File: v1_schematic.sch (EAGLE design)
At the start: 114 parts, among them IC1 PCA82C250, IC2 FT232RL, IC3 SP3223EBP, IC4 MAX481CPA, IC5 LM2576T, Q1 25MHz, Q2 32.768kHz, Q3 2N2222A, T1 ST02-3.5MM, T3 2N2222, T4 2N2222, T5 2N2222, T6 2N2222, T7 2N2222, U1 ON_SEMICONDUCTOR_NCP1117ST33T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, U2 ON_SEMICONDUCTOR_NCP1117ST50T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, X1 MINI-USB-32005-201

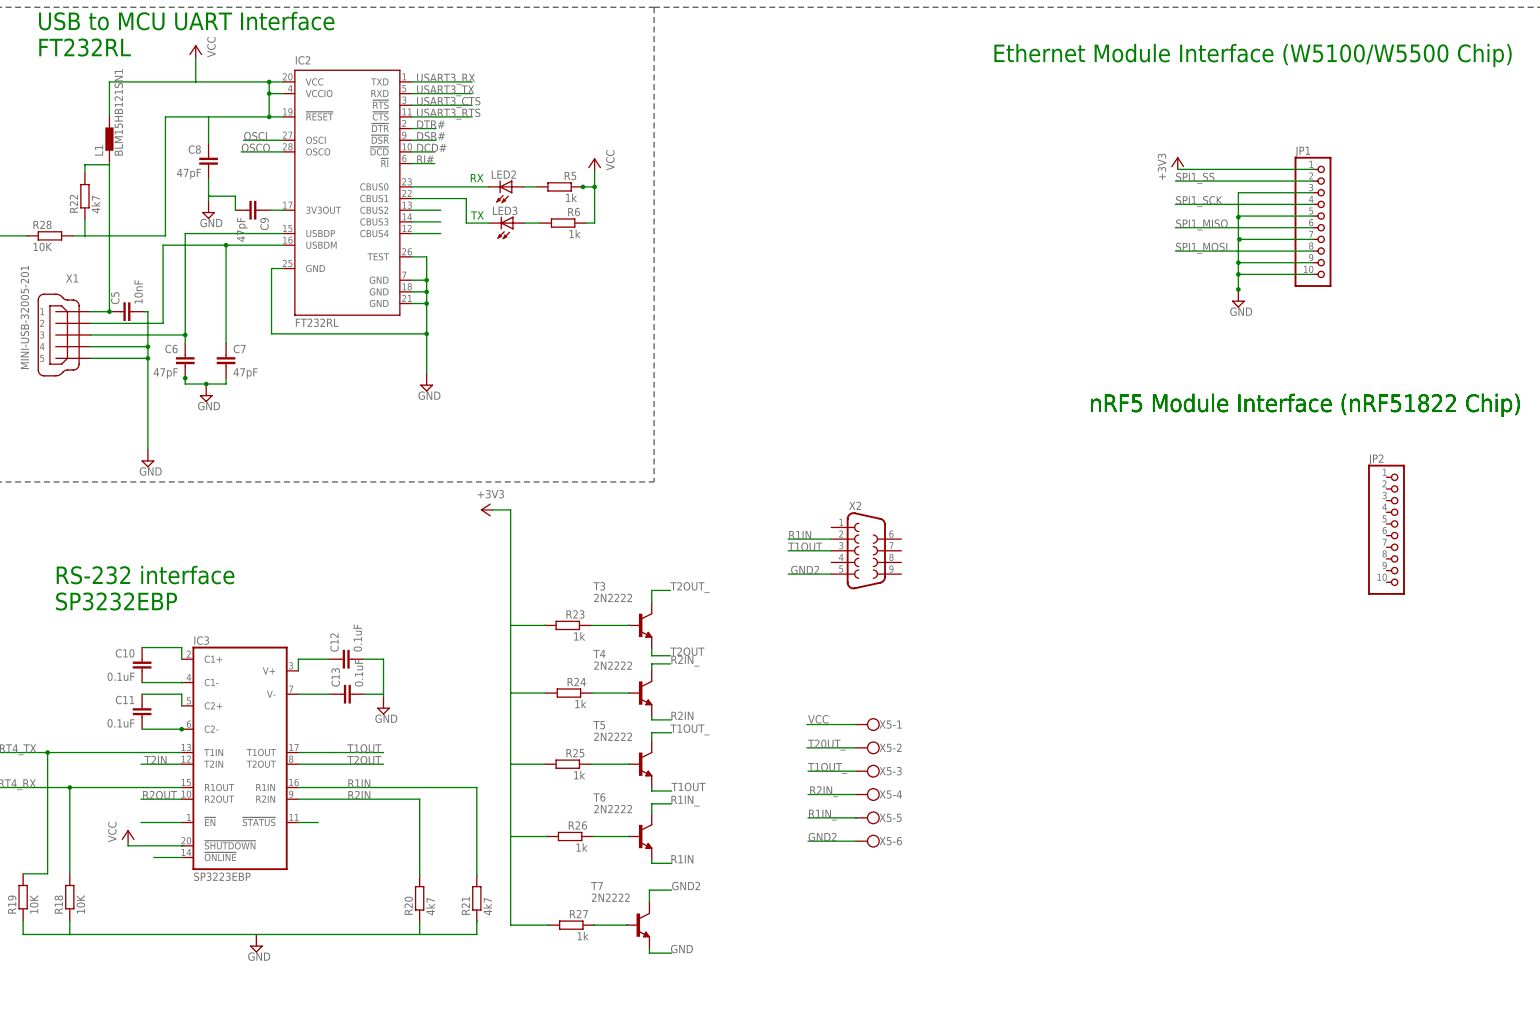
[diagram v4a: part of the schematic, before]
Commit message: SD Card Interface
- Added SD card interface based on
SD MEMORY CARD PUSH-PUSH WITH CONNECTOR TYPE B
Package Type: SDBMF-009XXBXX2
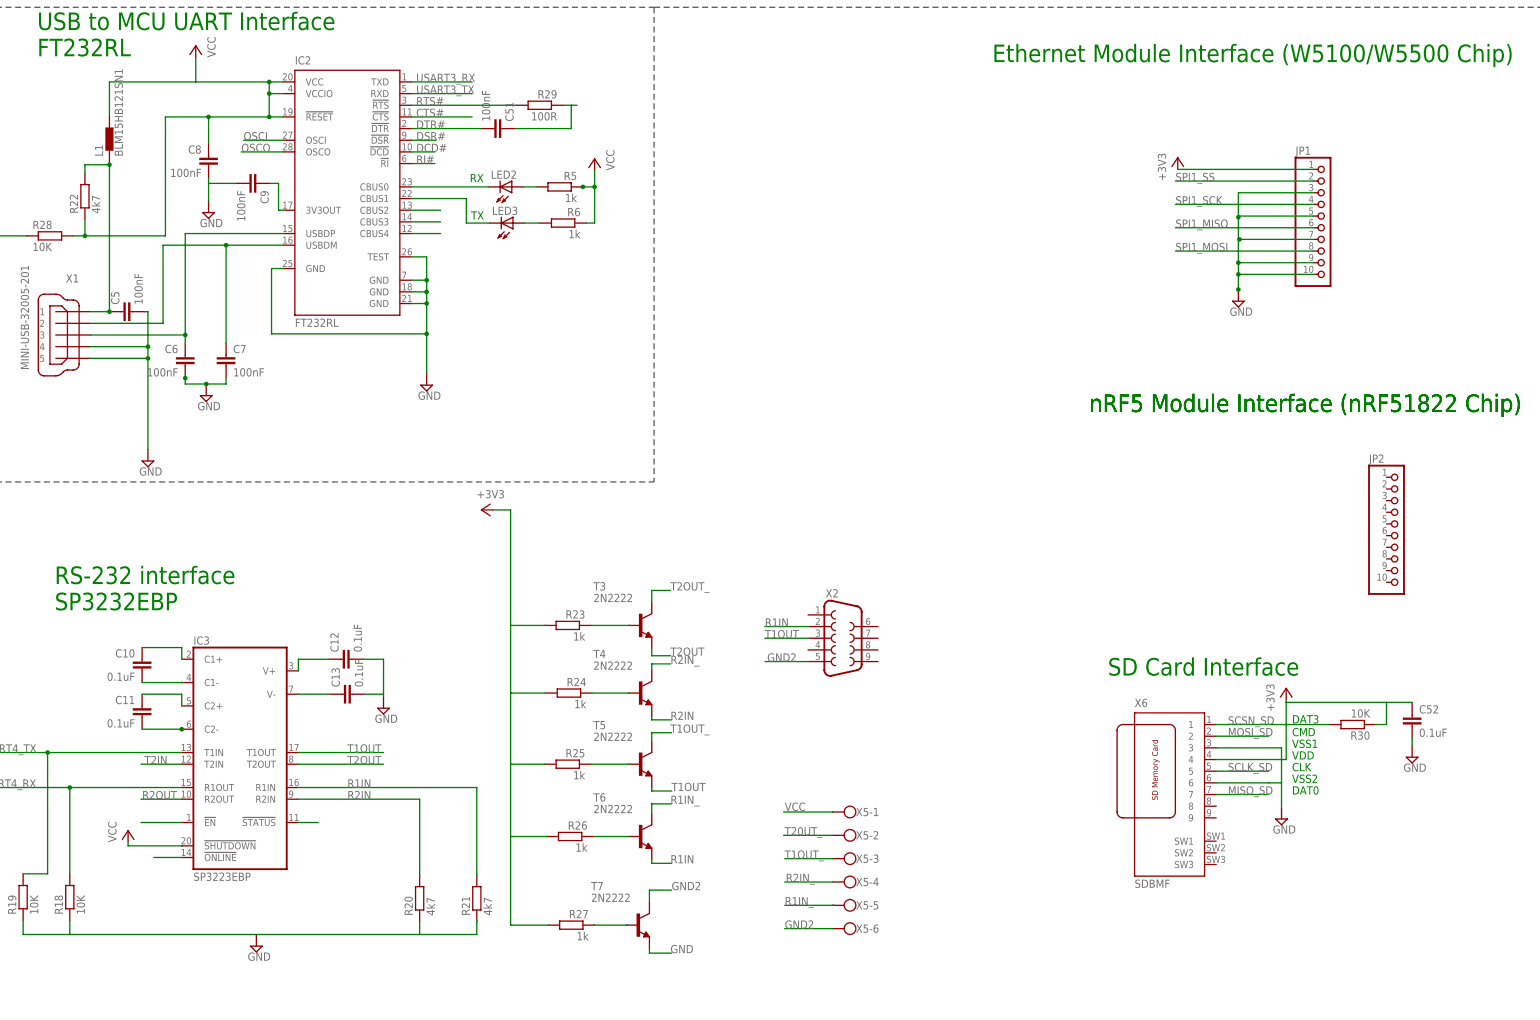
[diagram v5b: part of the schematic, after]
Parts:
- added C51: 100nF, resistor:C-EUC0805
- added C52: 0.1uF, resistor:C-EUC0805
- added R29: 100R, resistor:R-EU_R0805
- added R30: 10K, rcl:R-EU_R0805
- added X6: SDBMF, farnell:SDBMF
- C5: value 10nF -> 100nF
- C6, C7, C8, C9: value 47pF -> 100nF
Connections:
- new net CTS#: IC2.!CTS
- new net MISO_SD: X6.7
- new net MOSI_SD: X6.2
- new net RTS#: IC2.!RTS, R29.2
- new net SCLK_SD: X6.5
- new net SCSN_SD: R30.2, X6.1
- net +3V3: now also C52.1, R30.1, X6.4
- net DTR#: now also C51.2
- net GND: now also C52.2, X6.3, X6.6
- net N$31: now also C51.1, R29.1; no longer R22.1, R28.2
- net N$9: now also IC2.3V3OUT
- net USART3_CTS: no longer IC2.!RTS
- net USART3_RTS: no longer IC2.!CTS
- net VCC: now also R22.1, R28.2
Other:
- note added: "CLK"
- note added: "CMD"
- note added: "DAT0"
- note added: "DAT3"
- note added: "SD Card Interface"
- note added: "VDD"
- note added: "VSS1"
- note added: "VSS2"
- moved on the sheet: C9, X2, X5-1, X5-2, X5-3, X5-4, X5-5, X5-6

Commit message: Corrections
- Adjusted FT2323 interface to USART1 and completed Interface connections
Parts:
- removed JP1, JP2: (no value), pinhead:PINHD-1X10
- added X7, X8: 5566-8, con-molex:5566-8
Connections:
- removed net N$1: U$1.NRST
- removed net N$31: C51.1, R29.1
- removed net SPI1_MISO: JP1.6, U$1.PA6
- removed net SPI1_MOSI: JP1.8, U$1.PA7
- removed net SPI1_SCK: JP1.4, U$1.PA5
- removed net SPI1_SS: JP1.2, U$1.PA4
- new net ETH_MISO: U$1.PA6, X8-7.S
- new net ETH_MOSI: U$1.PA7, X8-6.S
- new net ETH_SCK: U$1.PA5, X8-4.S
- new net ETH_SS: U$1.PA4, X8-3.S
- new net NRF_CE: X7-3.S
- new net NRF_CS: X7-4.S
- new net NRF_IRQ: X7-8.S
- new net NRF_MISO: X7-7.S
- new net NRF_MOSI: X7-6.S
- new net NRF_SCK: X7-5.S
- new net RESET: C51.1, R29.1, U$1.NRST
- net +3V3: now also X7-2.S; no longer JP1.1
- net GND: now also X7-1.S; no longer JP1.10, JP1.3, JP1.5, JP1.7, JP1.9
- net R1IN: no longer X2.2
- net R1IN_: now also X2.2
- net T1OUT: no longer X2.3
- net T1OUT_: now also X2.3
- net USART1_RX: now also IC2.TXD
- net USART1_TX: now also IC2.RXD
- net USART3_RX: no longer IC2.TXD
- net USART3_TX: no longer IC2.RXD
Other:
- moved on the sheet: R4, R7, S1, S3

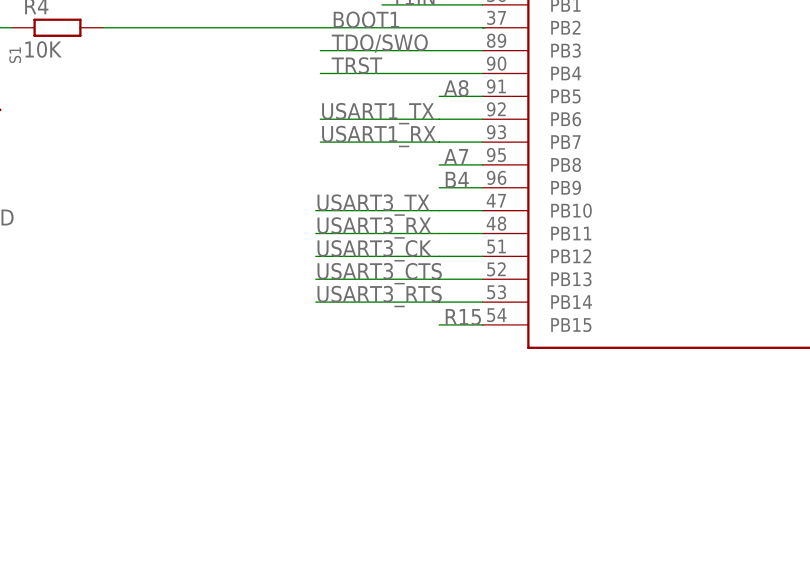
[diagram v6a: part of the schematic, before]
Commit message: Ethernet
-Connected Ethernet interface to SPI2 - PB12-PB15
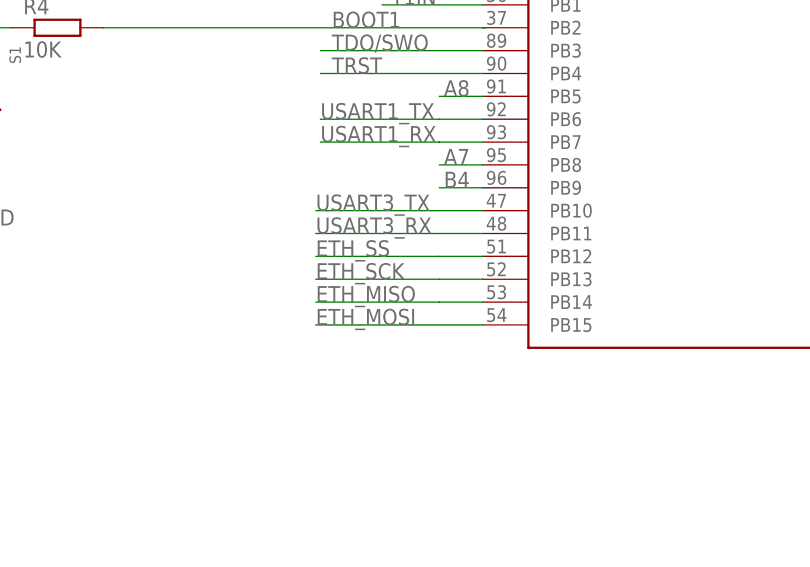
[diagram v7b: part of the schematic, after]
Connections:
- removed net R15: U$1.PB15
- removed net USART3_CK: U$1.PB12
- removed net USART3_CTS: U$1.PB13
- removed net USART3_RTS: U$1.PB14
- net ETH_MISO: now also U$1.PB14
- net ETH_MOSI: now also U$1.PB15
- net ETH_SCK: now also U$1.PB13
- net ETH_SS: now also U$1.PB12
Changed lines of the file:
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@@
 <pinref part="X8" gate="-3" pin="S"/>
+</segment>
+<segment>
+<pinref part="U$1" gate="G$1" pin="PB12"/>
+<wire x1="-209.296" y1="-57.404" x2="-214.122" y2="-57.404" width="0.1524" layer="91"/>
+<label x="-227.838" y="-57.404" size="1.778" layer="95"/>
+<wire x1="-214.122" y1="-57.404" x2="-227.838" y2="-57.404" width="0.15" layer="91"/>
 </segment>
 </net>
@@
 <label x="173.228" y="71.882" size="1.778" layer="95"/>
 <pinref part="X8" gate="-7" pin="S"/>
+</segment>
+<segment>
+<pinref part="U$1" gate="G$1" pin="PB14"/>
+<wire x1="-209.296" y1="-62.484" x2="-214.122" y2="-62.484" width="0.1524" layer="91"/>
+<label x="-227.838" y="-62.484" size="1.778" layer="95"/>
+<wire x1="-214.122" y1="-62.484" x2="-227.838" y2="-62.484" width="0.15" layer="91"/>
 </segment>
 </net>
@@
 <pinref part="X8" gate="-6" pin="S"/>
 </segment>
+<segment>
+<pinref part="U$1" gate="G$1" pin="PB15"/>
+<label x="-227.838" y="-65.024" size="1.778" layer="95"/>
+<wire x1="-209.296" y1="-65.024" x2="-227.838" y2="-65.024" width="0.1524" layer="91"/>
+</segment>
 </net>
 <net name="F15" class="0">
@@
 <label x="-227.838" y="-54.864" size="1.778" layer="95"/>
 <wire x1="-214.122" y1="-54.864" x2="-227.838" y2="-54.864" width="0.15" layer="91"/>
-</segment>
-</net>
-<net name="USART3_CK" class="0">
-<segment>
-<pinref part="U$1" gate="G$1" pin="PB12"/>
-<wire x1="-209.296" y1="-57.404" x2="-214.122" y2="-57.404" width="0.1524" layer="91"/>
-<label x="-227.838" y="-57.404" size="1.778" layer="95"/>
-<wire x1="-214.122" y1="-57.404" x2="-227.838" y2="-57.404" width="0.15" layer="91"/>
-</segment>
-</net>
-<net name="USART3_CTS" class="0">
-<segment>
-<pinref part="U$1" gate="G$1" pin="PB13"/>
-<wire x1="-209.296" y1="-59.944" x2="-214.122" y2="-59.944" width="0.1524" layer="91"/>
-<label x="-227.838" y="-59.944" size="1.778" layer="95"/>
-<wire x1="-214.122" y1="-59.944" x2="-227.838" y2="-59.944" width="0.15" layer="91"/>
-</segment>
-</net>
-<net name="USART3_RTS" class="0">
-<segment>
-<pinref part="U$1" gate="G$1" pin="PB14"/>
-<wire x1="-209.296" y1="-62.484" x2="-214.122" y2="-62.484" width="0.1524" layer="91"/>
-<label x="-227.838" y="-62.484" size="1.778" layer="95"/>
-<wire x1="-214.122" y1="-62.484" x2="-227.838" y2="-62.484" width="0.15" layer="91"/>
-</segment>
-</net>
-<net name="R15" class="0">
-<segment>
-<pinref part="U$1" gate="G$1" pin="PB15"/>
-<wire x1="-209.296" y1="-65.024" x2="-214.122" y2="-65.024" width="0.1524" layer="91"/>
-<label x="-213.614" y="-65.024" size="1.778" layer="95"/>
 </segment>
 </net>
@@
 <label x="-227.076" y="3.556" size="1.778" layer="95"/>
 </segment>
-</net>
+<segment>
+<pinref part="U$1" gate="G$1" pin="PB13"/>
+<wire x1="-209.296" y1="-59.944" x2="-214.122" y2="-59.944" width="0.1524" layer="91"/>
+<label x="-227.838" y="-59.944" size="1.778" layer="95"/>
+<wire x1="-214.122" y1="-59.944" x2="-227.838" y2="-59.944" width="0.15" layer="91"/>
+</segment>
+</net>

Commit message: SD Interface
- Completed SD interfacing to SDIO of MCU (PD2, PC8-PC12)
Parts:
- added R31, R32, R33, R34, R35: 10K, rcl:R-EU_R0805
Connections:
- removed net A12: U$1.PC12
- removed net B13: U$1.PC11
- removed net B14: U$1.PC10
- removed net D12: U$1.PD2
- removed net F14: U$1.PC9
- removed net G14: U$1.PC8
- removed net MISO_SD: X6.7
- removed net MOSI_SD: X6.2
- removed net SCLK_SD: X6.5
- removed net SCSN_SD: R30.2, X6.1
- new net N$31: X6.3, X6.6
- new net SD_CMD: R31.2, U$1.PD2, X6.2
- new net SD_D0: U$1.PC8, X6.7
- new net SD_D1: U$1.PC9, X6.8
- new net SD_D2: U$1.PC10, X6.9
- new net SD_D3: R32.2, U$1.PC11, X6.1
- new net SD_SCK: R30.2, U$1.PC12, X6.5
- net +3V3: now also R31.1, R32.1, R34.2, R35.2
- net GND: no longer X6.3, X6.6
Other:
- note removed: "CLK"
- note removed: "CMD"
- note removed: "DAT0"
- note removed: "DAT3"
- note removed: "VDD"
- note removed: "VSS1"
- note removed: "VSS2"
- moved on the sheet: C52, R30
